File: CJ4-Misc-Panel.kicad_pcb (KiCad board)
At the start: 2 copper layers, 122 x 57 mm, 63 parts, among them J1 USB_B_Micro, J2 Conn_01x02, J3 RP2040_SWD, J4 TC2030-IDC-NL, SW1 SW_PUSH_LED, SW10 SW_PUSH_LED, SW11 SW_PUSH_LED, SW12 SW_PUSH_LED, SW13 SW_PUSH_LED, SW14 SW_PUSH_LED, SW15 SW_PUSH_LED, SW16 SW_PUSH_LED, SW17 SW_PUSH_LED, SW18 SW_PUSH_LED, SW19 SW_PUSH_LED, SW2 SW_PUSH_LED, SW20 SW_PUSH_LED, SW21 SW_PUSH_LED, SW22 SW_PUSH_LED, SW3 SW_PUSH_LED, SW4 SW_PUSH_LED, SW5 SW_PUSH_LED, SW6 SW_PUSH_LED, SW7 SW_PUSH_LED, SW8 SW_PUSH_LED, SW9 SW_PUSH_LED, U1 RP2040, U2 AMS1117-3.3, U3 W25Q128JVS, U4 DM13A, U5 DM13A, Y1 X322512MSB4SI

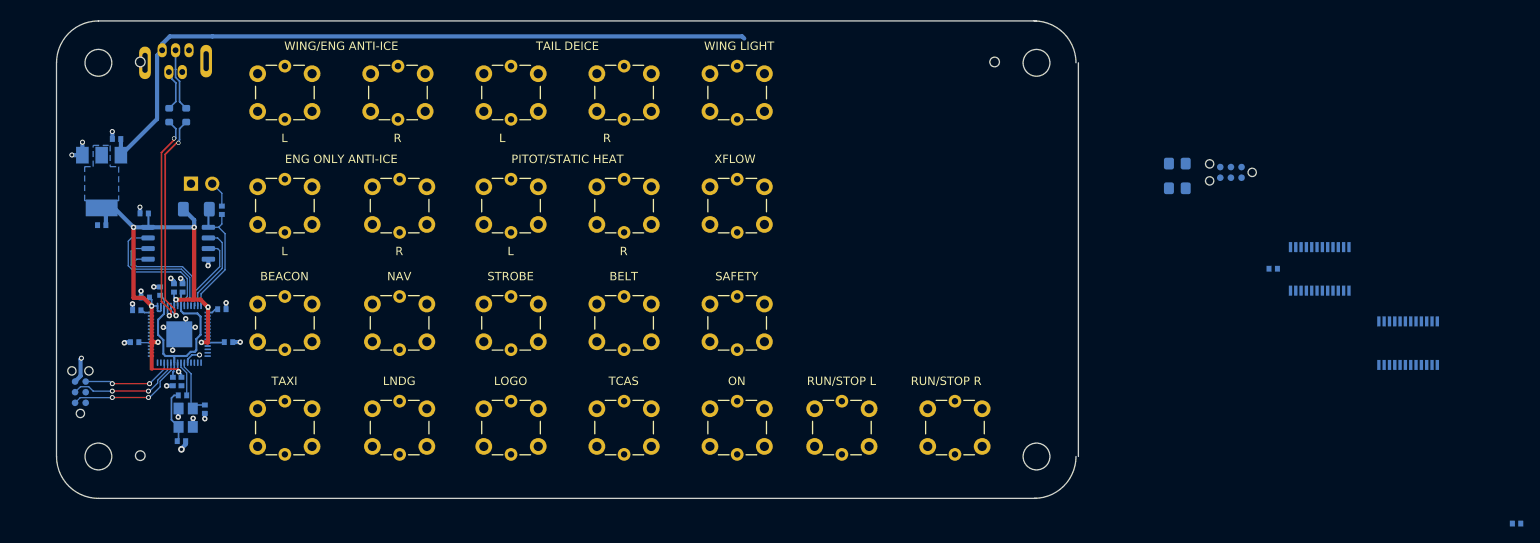
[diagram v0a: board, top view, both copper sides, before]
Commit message: All the buttons are routed. Ugly, but routed.
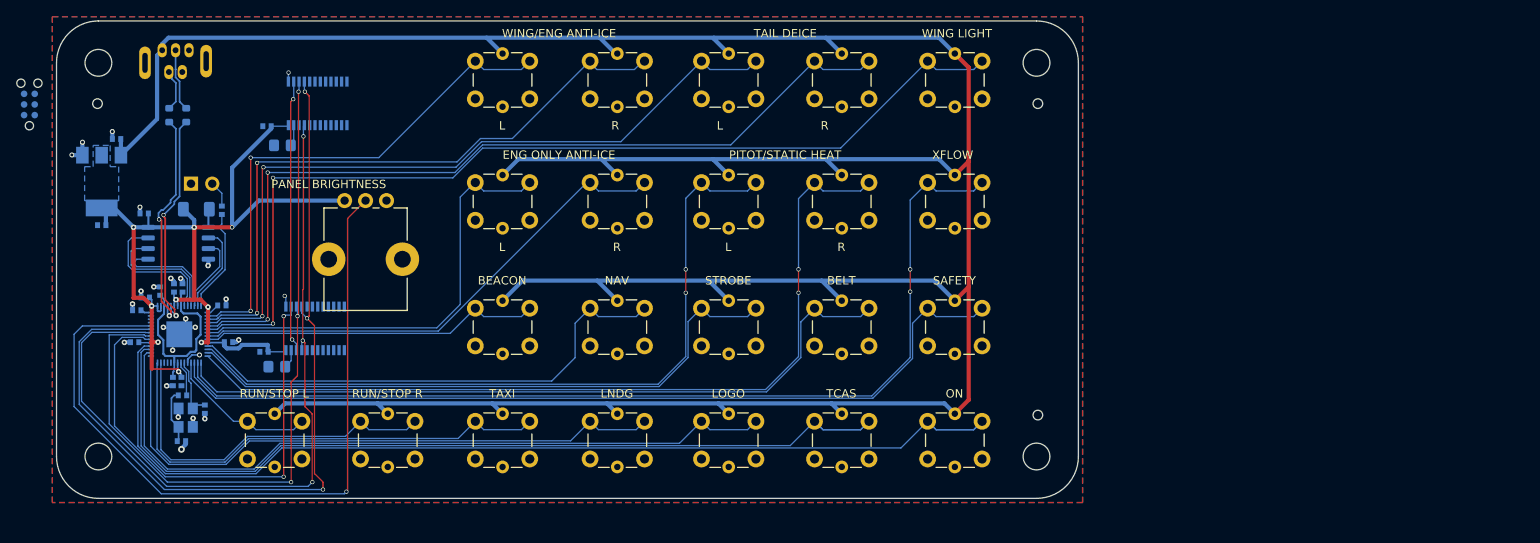
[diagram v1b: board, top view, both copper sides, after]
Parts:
- removed J3: RP2040_SWD, Connector:Tag-Connect_TC2030-IDC-NL_2x03_P1.27mm_Vertical
- added RV1: R_Potentiometer, Potentiometer_THT:Potentiometer_Bourns_PTV09A-1_Single_Vertical, F.Cu at (54.4, 41.4)
- moved C16 150.9 mm to (44.8, 59.5)
- moved J4 143.7 mm to (16.8, 30.0), turned to 90 degrees
- moved U4 130.5 mm to (50.9, 56.7)
- moved C17 121.3 mm to (45.1, 32.6)
- moved U5 121.3 mm to (51.2, 29.8)
- moved R7 109.6 mm to (46.3, 61.3)
- moved H6 107.3 mm to (137.2, 67.2)
- moved R6 106.9 mm to (47.0, 34.9)
- moved SW21 67.7 mm to (46.0, 70.0)
- moved SW2 57.9 mm to (86.9, 27.0)
- moved SW22 41.5 mm to (59.5, 70.0)
- moved SW1 26.0 mm to (73.2, 27.0)
- moved SW14 26.0 mm to (73.2, 70.0)
- moved SW15 26.0 mm to (86.9, 70.0)
- moved SW16 26.0 mm to (100.2, 70.0)
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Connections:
- net /RP2040/GPIO27 renamed /RP2040/GPIO27_ADC1
- net /RP2040/GPIO28 renamed /RP2040/GPIO28_ADC2
- net /RP2040/GPIO29 renamed /RP2040/GPIO29_ADC3
- U1 pad 11: /PITOT_2 -> /NAV
- U1 pad 12: /XFLOW -> /PITOT_1
- U1 pad 13: /BEACON -> /STROBE
- U1 pad 14: /NAV -> /PITOT_2
- U1 pad 15: /STROBE -> /PASS_BELT
- U1 pad 16: /TAXI -> /XFLOW
- U1 pad 17: /LNDG -> /PASS_SAFETY
- U1 pad 18: /LOGO -> /RUN_STOP_L
- U1 pad 24: /RP2040/SWD -> unconnected-(U1-Pad24)
- U1 pad 25: /RP2040/SWCLK -> unconnected-(U1-Pad25)
- U1 pad 26: /RP2040/~{RST} -> unconnected-(U1-Pad26)
- U1 pad 27: /PASS_BELT -> /RUN_STOP_R
- U1 pad 28: /PASS_SAFETY -> /TAXI
- U1 pad 29: /PULSE_TCAS -> /LNDG
- U1 pad 30: /PULSE_ON -> /LOGO
- U1 pad 31: /RUN_STOP_L -> /PULSE_TCAS
- U1 pad 32: /RUN_STOP_R -> /PULSE_ON
- U1 pad 36: /LED_LATCH -> /BRIGHTNESS
- U1 pad 37: /BRIGHTNESS -> /LED_LATCH
- U1 pad 38: /RP2040/GPIO26 -> /PANEL_BRIGHT
- U1 pad 9: /PITOT_1 -> /BEACON
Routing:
- net +5V: track 87.2 -> 393.5 mm
- net /PULSE_ON: track 0.00 -> 126.0 mm
- net /XFLOW: track 0.00 -> 118.7 mm, vias 0 -> 2
- net /WING_LIGHT: track 0.00 -> 116.7 mm, vias 0 -> 2
- net /PULSE_TCAS: track 0.00 -> 111.3 mm
- net /PASS_SAFETY: track 0.00 -> 104.5 mm
- net /TAIL_R: track 0.00 -> 103.1 mm, vias 0 -> 2
- net /PITOT_2: track 0.00 -> 102.7 mm, vias 0 -> 2
- net /LED_LATCH: track 0.00 -> 101.5 mm, vias 0 -> 3
- net /BRIGHTNESS: track 0.00 -> 92.0 mm, vias 0 -> 3
- net /PANEL_BRIGHT: track 0.00 -> 90.9 mm, vias 0 -> 1
- net /PASS_BELT: track 0.00 -> 89.6 mm
- net /TAIL_L: track 0.00 -> 89.5 mm, vias 0 -> 2
- net /LED_CLOCK: track 0.00 -> 89.5 mm, vias 0 -> 3
- net /LOGO: track 0.00 -> 89.1 mm
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- added copper zone on B.Cu, net GND
- added copper zone on F.Cu, net GND
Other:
- outline, holes or cut-outs redrawn
- board text added: "PANEL BRIGHTNESS"

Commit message: Fully routed!!!
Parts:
- moved J4 26.3 mm to (42.9, 27.1)
- renumbered R7 to R6, R6 to R7
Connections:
- J4 pad 1: /LED_LATCH -> /LED_DIN
- J4 pad 3: /LED_CLOCK -> unconnected-(J4-Pad3)
- J4 pad 4: unconnected-(J4-Pad4) -> /LED_CLOCK
- J4 pad 5: /LED_DIN -> GND
- J4 pad 6: GND -> /LED_LATCH
- R6 pad 1: /REXT -> /REXT_1
- R7 pad 1: /REXT -> /REXT_2
- U4 pad 10: /LED_ENG_ONLY_L -> unconnected-(U4-Pad10)
- U4 pad 11: /LED_ENG_ONLY_R -> unconnected-(U4-Pad11)
- U4 pad 12: /LED_PITOT_1 -> unconnected-(U4-Pad12)
- U4 pad 13: /LED_LOGO -> /LED_LNDG
- U4 pad 14: /LED_LNDG -> /LED_TAXI
- U4 pad 15: /LED_TAXI -> /LED_RUN_STOP_R
- U4 pad 16: /LED_STROBE -> /LED_RUN_STOP_L
- U4 pad 17: /LED_NAV -> /LED_LOGO
- U4 pad 18: /LED_BEACON -> /LED_PULSE_TCAS
- U4 pad 19: /LED_XFLOW -> /LED_PULSE_ON
- U4 pad 20: /LED_PITOT_2 -> unconnected-(U4-Pad20)
- U4 pad 23: /REXT -> /REXT_1
- U4 pad 5: /LED_WING_ENG_L -> unconnected-(U4-Pad5)
- U4 pad 6: /LED_WING_ENG_R -> unconnected-(U4-Pad6)
- U4 pad 7: /LED_TAIL_L -> unconnected-(U4-Pad7)
- U4 pad 8: /LED_TAIL_R -> unconnected-(U4-Pad8)
- U4 pad 9: /LED_WING_LIGHT -> unconnected-(U4-Pad9)
- U5 pad 10: /LED_RUN_STOP_R -> /LED_WING_ENG_R
- U5 pad 11: unconnected-(U5-Pad11) -> /LED_WING_ENG_L
- U5 pad 12: unconnected-(U5-Pad12) -> /LED_PITOT_1
- U5 pad 14: unconnected-(U5-Pad14) -> /LED_BEACON
- U5 pad 15: unconnected-(U5-Pad15) -> /LED_NAV
- U5 pad 16: unconnected-(U5-Pad16) -> /LED_STROBE
- U5 pad 17: unconnected-(U5-Pad17) -> /LED_PASS_BELT
- U5 pad 18: unconnected-(U5-Pad18) -> /LED_PASS_SAFETY
- U5 pad 19: unconnected-(U5-Pad19) -> /LED_ENG_ONLY_L
- U5 pad 20: unconnected-(U5-Pad20) -> /LED_ENG_ONLY_R
- U5 pad 23: /REXT -> /REXT_2
- U5 pad 5: /LED_PASS_BELT -> /LED_WING_LIGHT
- U5 pad 6: /LED_PASS_SAFETY -> /LED_XFLOW
- U5 pad 7: /LED_PULSE_TCAS -> /LED_TAIL_R
- U5 pad 8: /LED_PULSE_ON -> /LED_PITOT_2
- U5 pad 9: /LED_RUN_STOP_L -> /LED_TAIL_L
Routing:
- net /LED_PASS_SAFETY: track 0.00 -> 105.7 mm, vias 0 -> 3
- net /LED_XFLOW: track 0.00 -> 96.3 mm, vias 0 -> 1
- net /LED_PASS_BELT: track 0.00 -> 91.1 mm, vias 0 -> 3
- net /LED_PULSE_ON: track 0.00 -> 90.9 mm, vias 0 -> 1
- net /LED_WING_LIGHT: track 0.00 -> 83.1 mm
- net /LED_PITOT_2: track 0.00 -> 80.5 mm, vias 0 -> 1
- net /LED_PULSE_TCAS: track 0.00 -> 76.0 mm, vias 0 -> 1
- net /LED_STROBE: track 0.00 -> 75.8 mm, vias 0 -> 3
- net /LED_TAIL_R: track 0.00 -> 67.6 mm
- net /LED_LOGO: track 0.00 -> 61.3 mm, vias 0 -> 1
- net /LED_NAV: track 0.00 -> 61.0 mm, vias 0 -> 3
- net /LED_PITOT_1: track 0.00 -> 59.7 mm, vias 0 -> 1
- net /LED_ENG_ONLY_R: track 0.00 -> 52.9 mm, vias 0 -> 1
- net /LED_TAIL_L: track 0.00 -> 50.6 mm
- net /LED_BEACON: track 0.00 -> 46.0 mm, vias 0 -> 3
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
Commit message: Cleanly routed
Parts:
- moved C13 0.46 mm to (40.5, 58.8)
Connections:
- U1 pad 7: /ENG_ONLY_L -> /BEACON
- U1 pad 8: /ENG_ONLY_R -> /ENG_ONLY_L
- U1 pad 9: /BEACON -> /ENG_ONLY_R
- U4 pad 10: unconnected-(U4-Pad10) -> /LED_NAV
- U4 pad 11: unconnected-(U4-Pad11) -> /LED_STROBE
- U4 pad 5: unconnected-(U4-Pad5) -> /LED_ENG_ONLY_L
- U4 pad 6: unconnected-(U4-Pad6) -> /LED_ENG_ONLY_R
- U4 pad 7: unconnected-(U4-Pad7) -> /LED_PASS_SAFETY
- U4 pad 8: unconnected-(U4-Pad8) -> /LED_PASS_BELT
- U4 pad 9: unconnected-(U4-Pad9) -> /LED_BEACON
- U5 pad 10: /LED_WING_ENG_R -> /LED_WING_ENG_L
- U5 pad 11: /LED_WING_ENG_L -> /LED_PITOT_1
- U5 pad 12: /LED_PITOT_1 -> /LED_TAIL_L
- U5 pad 14: /LED_BEACON -> unconnected-(U5-Pad14)
- U5 pad 15: /LED_NAV -> unconnected-(U5-Pad15)
- U5 pad 16: /LED_STROBE -> unconnected-(U5-Pad16)
- U5 pad 17: /LED_PASS_BELT -> unconnected-(U5-Pad17)
- U5 pad 18: /LED_PASS_SAFETY -> unconnected-(U5-Pad18)
- U5 pad 19: /LED_ENG_ONLY_L -> unconnected-(U5-Pad19)
- U5 pad 20: /LED_ENG_ONLY_R -> unconnected-(U5-Pad20)
- U5 pad 9: /LED_TAIL_L -> /LED_WING_ENG_R
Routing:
- net /LED_BEACON: track 46.0 -> 30.5 mm, vias 3 -> 1
- net /LED_PASS_BELT: track 91.1 -> 77.3 mm, vias 3 -> 1
- net /LED_STROBE: track 75.8 -> 62.3 mm, vias 3 -> 1
- net /LED_PASS_SAFETY: track 105.7 -> 92.3 mm, vias 3 -> 1
- net /LED_ENG_ONLY_R: track 52.9 -> 40.9 mm, vias 1 -> 0
- net /LED_NAV: track 61.0 -> 49.3 mm, vias 3 -> 1
- net +5V: track 393.5 -> 383.5 mm
- net /LED_ENG_ONLY_L: track 37.8 -> 27.8 mm, vias 1 -> 0
- net /PULSE_TCAS: track 111.3 -> 101.8 mm
- net /PULSE_ON: track 126.0 -> 116.8 mm
- net GND: track 30.2 -> 37.6 mm, vias 30 -> 277
- net /LED_LATCH: track 108.8 -> 103.4 mm
- net /ENG_ONLY_R: track 66.0 -> 70.8 mm
- net /LED_LNDG: track 44.1 -> 48.2 mm
- net /BRIGHTNESS: track 100.2 -> 96.1 mm
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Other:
- board text added: "${VERSION}"
- board text added: "CJ4 PFD misc panel Neil Enns neile@live.com ${DATE} ${VERSION}"

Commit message: Final routing, updated JLCPCB rotations
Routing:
- net /LED_DIN: track 86.8 -> 84.6 mm
- net /LED_LATCH: track 103.4 -> 102.1 mm
- net +5V: track 383.5 -> 384.6 mm
- net /BRIGHTNESS: track 96.1 -> 95.1 mm
- net /LED_CLOCK: track 95.6 -> 94.8 mm
- net /PANEL_BRIGHT: track 87.7 -> 87.0 mm
- net GND: track 37.6 -> 37.4 mm, vias 277 -> 276

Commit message: Add JLC order number placement
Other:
- board text added: "JLCJLCJLCJLC"
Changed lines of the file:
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@@
+    (effects (font (size 1 1) (thickness 0.15)))
+  )
+  (gr_text "JLCJLCJLCJLC" (at 57 48.2 90) (layer "F.SilkS")
     (effects (font (size 1 1) (thickness 0.15)))
   )
@@
   (segment (start 51.1895 59.306) (end 51.1895 58.556) (width 0.15) (layer "B.Cu") (net 59))
   (segment (start 112.4505 56.8) (end 112.6 56.9495) (width 0.15) (layer "B.Cu") (net 59))
+  (segment (start 33.8 73.8) (end 39.4 73.8) (width 0.15) (layer "B.Cu") (net 60))
   (segment (start 29.8 59.8) (end 29.8 69.8) (width 0.15) (layer "B.Cu") (net 60))
   (segment (start 42.2 71) (end 120.798 71) (width 0.15) (layer "B.Cu") (net 60))
-  (segment (start 39.4 73.8) (end 42.2 71) (width 0.15) (layer "B.Cu") (net 60))
   (segment (start 31.275466 58.8122) (end 30.7878 58.8122) (width 0.15) (layer "B.Cu") (net 60))
-  (segment (start 33.8 73.8) (end 39.4 73.8) (width 0.15) (layer "B.Cu") (net 60))
   (segment (start 124.202 68) (end 130.298 68) (width 0.15) (layer "B.Cu") (net 60))
   (segment (start 30.7878 58.8122) (end 29.8 59.8) (width 0.15) (layer "B.Cu") (net 60))
   (segment (start 29.8 69.8) (end 33.8 73.8) (width 0.15) (layer "B.Cu") (net 60))
+  (segment (start 39.4 73.8) (end 42.2 71) (width 0.15) (layer "B.Cu") (net 60))
   (segment (start 120.798 71) (end 124 67.798) (width 0.15) (layer "B.Cu") (net 60))
   (segment (start 127.25 73.248) (end 126.2 72.198) (width 0.15) (layer "F.Cu") (net 61))
